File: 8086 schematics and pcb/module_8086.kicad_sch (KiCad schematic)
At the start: 1 part, among them U1 P8086-2

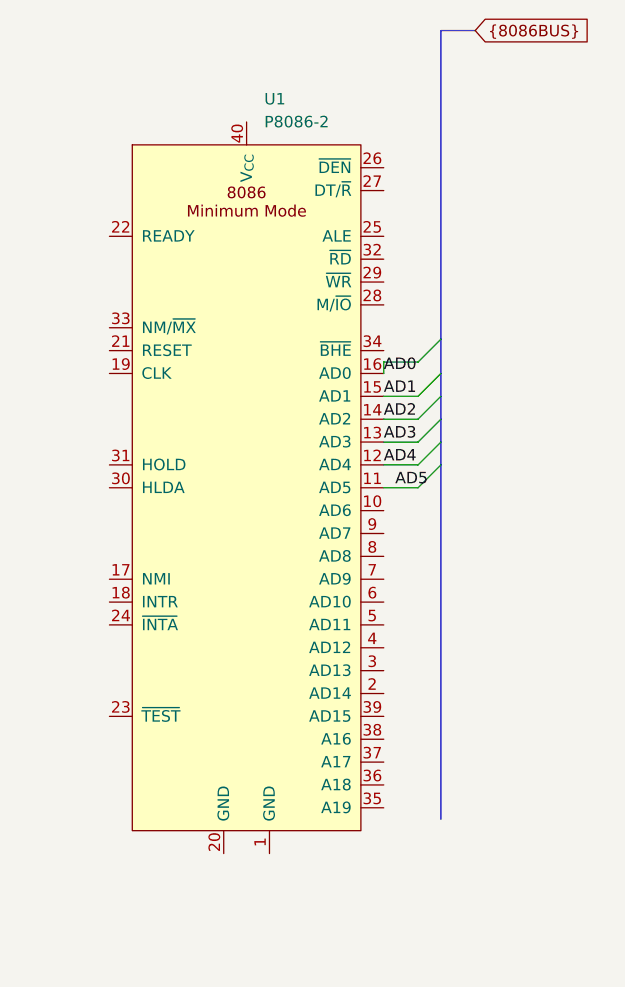
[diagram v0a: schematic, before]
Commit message: 8086 module - bus connected
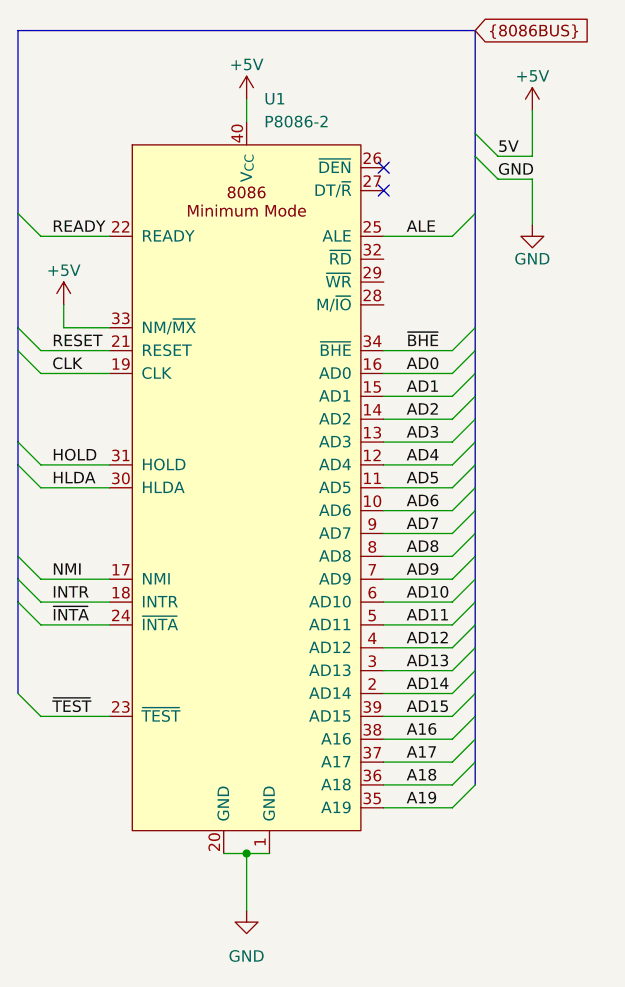
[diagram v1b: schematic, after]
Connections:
- net GND: now reaches U1.1 (GND)
- net GND: now also U1.20 (GND)
- net AD6: now reaches U1.10 (AD6)
- net NMI: now reaches U1.17 (NMI)
- net INTR: now reaches U1.18 (INTR)
- net CLK: now reaches U1.19 (CLK)
- net AD14: now reaches U1.2 (AD14)
- net RESET: now reaches U1.21 (RESET)
- net READY: now reaches U1.22 (READY)
- net ~{TEST}: now reaches U1.23 (~{TEST})
- net ~{INTA}: now reaches U1.24 (~{INTA})
- net ALE: now reaches U1.25 (ALE)
- net AD13: now reaches U1.3 (AD13)
- net HLDA: now reaches U1.30 (HLDA)
- net HOLD: now reaches U1.31 (HOLD)
- net +5V: now reaches U1.33 (NM/~{MX})
- net +5V: now also U1.40 (V_{CC})
- net ~{BHE}: now reaches U1.34 (~{BHE})
- net A19: now reaches U1.35 (A19)
- net A18: now reaches U1.36 (A18)
- net A17: now reaches U1.37 (A17)
- net A16: now reaches U1.38 (A16)
- net AD15: now reaches U1.39 (AD15)
- net AD12: now reaches U1.4 (AD12)
- net AD11: now reaches U1.5 (AD11)
- net AD10: now reaches U1.6 (AD10)
- net AD9: now reaches U1.7 (AD9)
- net AD8: now reaches U1.8 (AD8)
- net AD7: now reaches U1.9 (AD7)
- no-connect marks 0 -> 2

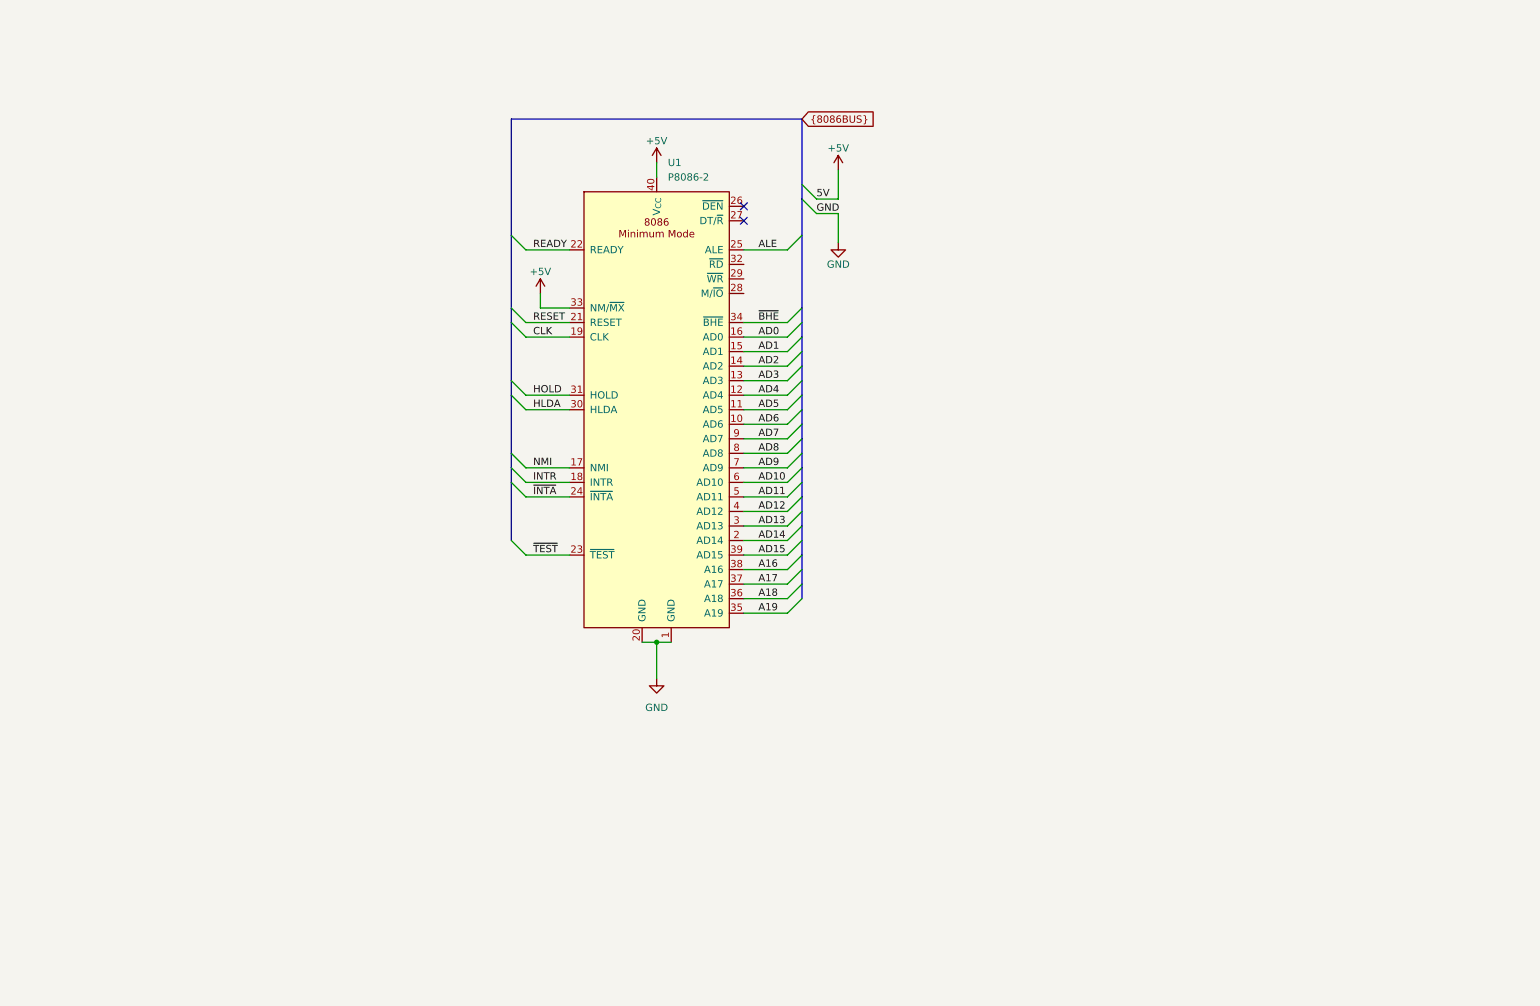
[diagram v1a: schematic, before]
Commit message: 8086 module - address latches, start of memory ICs
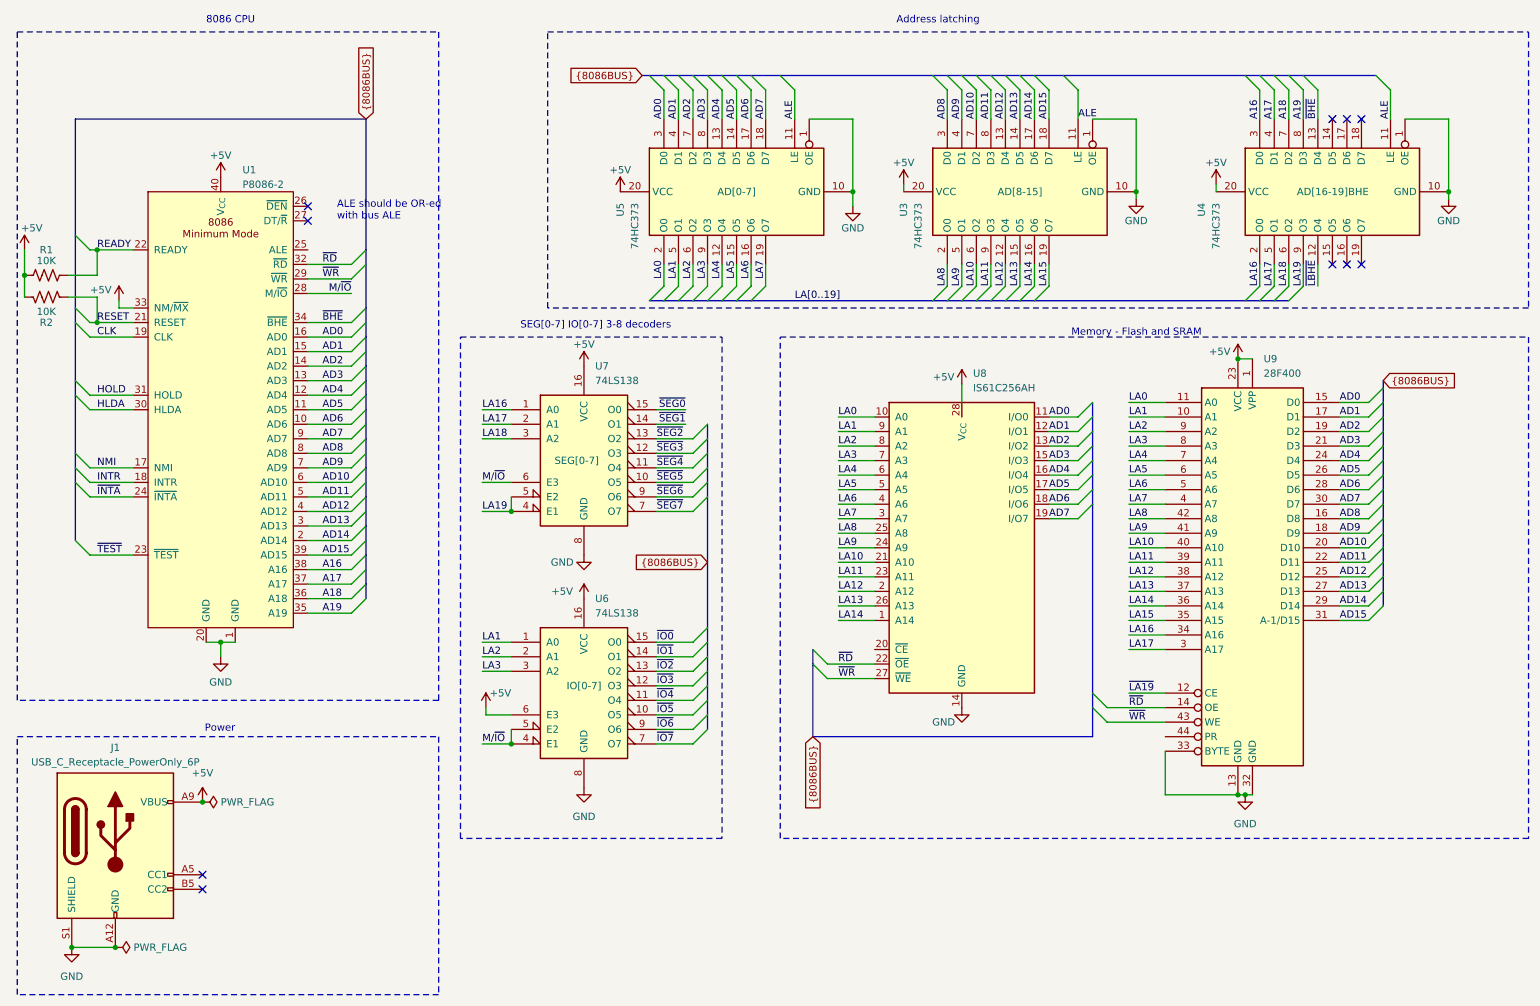
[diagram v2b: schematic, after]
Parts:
- added J1: USB_C_Receptacle_PowerOnly_6P, symbol Connector:USB_C_Receptacle_PowerOnly_6P
- added R1, R2: 10K, symbol Device:R_US
- added U3, U4, U5: 74HC373, symbol 74xx:74HC373
- added U6, U7: 74LS138, symbol 74xx:74LS138
- added U8: IS61C256AH, Package_SO:TSOP-I-28_11.8x8mm_P0.55mm, symbol 8086PC:IS61C256AH
- added U9: 28F400, Package_SO:PSOP-44_16.9x27.17mm_P1.27mm, symbol Memory_Flash:28F400
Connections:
- net +5V: now also J1.A9 (VBUS), J1.B9 (VBUS), R1.1, R2.1, U3.20 (VCC), U4.20 (VCC), U5.20 (VCC), U6.16 (VCC), U6.6 (E3), U7.16 (VCC), U8.28 (V_{CC}), U9.1 (VPP), U9.23 (VCC)
- net A16: now also U4.3 (D0)
- net A17: now also U4.4 (D1)
- net A18: now also U4.7 (D2)
- net A19: now also U4.8 (D3)
- net AD0: now also U5.3 (D0), U8.11 (I/O0), U9.15 (D0)
- net AD1: now also U5.4 (D1), U8.12 (I/O1), U9.17 (D1)
- net AD10: now also U3.7 (D2), U9.20 (D10)
- net AD11: now also U3.8 (D3), U9.22 (D11)
- net AD12: now also U3.13 (D4), U9.25 (D12)
- net AD13: now also U3.14 (D5), U9.27 (D13)
- net AD14: now also U3.17 (D6), U9.29 (D14)
- net AD15: now also U3.18 (D7), U9.31 (A-1/D15)
- net AD2: now also U5.7 (D2), U8.13 (I/O2), U9.19 (D2)
- net AD3: now also U5.8 (D3), U8.15 (I/O3), U9.21 (D3)
- net AD4: now also U5.13 (D4), U8.16 (I/O4), U9.24 (D4)
- net AD5: now also U5.14 (D5), U8.17 (I/O5), U9.26 (D5)
- net AD6: now also U5.17 (D6), U8.18 (I/O6), U9.28 (D6)
- net AD7: now also U5.18 (D7), U8.19 (I/O7), U9.30 (D7)
- net AD8: now also U3.3 (D0), U9.16 (D8)
- net AD9: now also U3.4 (D1), U9.18 (D9)
- net ALE: now also U3.11 (LE), U4.11 (LE), U5.11 (LE); no longer U1.25 (ALE)
- net GND: now also J1.A12 (GND), J1.B12 (GND), J1.S1 (SHIELD), U3.1 (OE), U3.10 (GND), U4.1 (OE), U4.10 (GND), U5.1 (OE), U5.10 (GND), U6.8 (GND), U7.8 (GND), U8.14 (GND), U9.13 (GND), U9.32 (GND), U9.33 (BYTE)
- net READY: now also R1.2
- net RESET: now also R2.2
- net ~{BHE}: now also U4.13 (D4)
- net M/~{IO}: now reaches U1.28 (M/~{IO})
- net M/~{IO}: now also U6.4 (E1), U6.5 (E2), U7.6 (E3)
- net ~{WR}: now reaches U1.29 (~{WR})
- net ~{WR}: now also U8.27 (~{WE}), U9.43 (WE)
- net ~{RD}: now reaches U1.32 (~{RD})
- net ~{RD}: now also U8.22 (~{OE}), U9.14 (OE)
- new net LA0: U5.2 (O0), U8.10 (A0), U9.11 (A0)
- new net LA1: U5.5 (O1), U6.1 (A0), U8.9 (A1), U9.10 (A1)
- new net LA10: U3.6 (O2), U8.21 (A10), U9.40 (A10)
- new net LA11: U3.9 (O3), U8.23 (A11), U9.39 (A11)
- new net LA12: U3.12 (O4), U8.2 (A12), U9.38 (A12)
- new net LA13: U3.15 (O5), U8.26 (A13), U9.37 (A13)
- new net LA14: U3.16 (O6), U8.1 (A14), U9.36 (A14)
- new net LA15: U3.19 (O7), U9.35 (A15)
- new net LA16: U4.2 (O0), U7.1 (A0), U9.34 (A16)
- new net LA17: U4.5 (O1), U7.2 (A1), U9.3 (A17)
- new net LA18: U4.6 (O2), U7.3 (A2)
- new net LA19: U4.9 (O3), U7.4 (E1), U7.5 (E2)
- new net LA2: U5.6 (O2), U6.2 (A1), U8.8 (A2), U9.9 (A2)
- new net LA3: U5.9 (O3), U6.3 (A2), U8.7 (A3), U9.8 (A3)
- new net LA4: U5.12 (O4), U8.6 (A4), U9.7 (A4)
- new net LA5: U5.15 (O5), U8.5 (A5), U9.6 (A5)
- new net LA6: U5.16 (O6), U8.4 (A6), U9.5 (A6)
- new net LA7: U5.19 (O7), U8.3 (A7), U9.4 (A7)
- new net LA8: U3.2 (O0), U8.25 (A8), U9.42 (A8)
- new net LA9: U3.5 (O1), U8.24 (A9), U9.41 (A9)
- new net ~{IO0}: U6.15 (O0)
- new net ~{IO1}: U6.14 (O1)
- new net ~{IO2}: U6.13 (O2)
- new net ~{IO3}: U6.12 (O3)
- new net ~{IO4}: U6.11 (O4)
- new net ~{IO5}: U6.10 (O5)
- new net ~{IO6}: U6.9 (O6)
- new net ~{IO7}: U6.7 (O7)
- new net ~{LA19}: U9.12 (CE)
- new net ~{LBHE}: U4.12 (O4)
- new net ~{SEG0}: U7.15 (O0)
- new net ~{SEG1}: U7.14 (O1)
- new net ~{SEG2}: U7.13 (O2)
- new net ~{SEG3}: U7.12 (O3)
- new net ~{SEG4}: U7.11 (O4)
- new net ~{SEG5}: U7.10 (O5)
- new net ~{SEG6}: U7.9 (O6)
- new net ~{SEG7}: U7.7 (O7)
- no-connect marks 2 -> 10
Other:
- note added: "8086 CPU"
- note added: "ALE should be OR-ed with bus ALE"
- note added: "Address latching"
- note added: "Memory - Flash and SRAM"
- note added: "Power"
- note added: "SEG[0-7] IO[0-7] 3-8 decoders"
- moved on the sheet: U1
